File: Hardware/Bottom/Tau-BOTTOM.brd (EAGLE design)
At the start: 33 x 33 mm, 31 parts, among them U1 AD5242-SO16

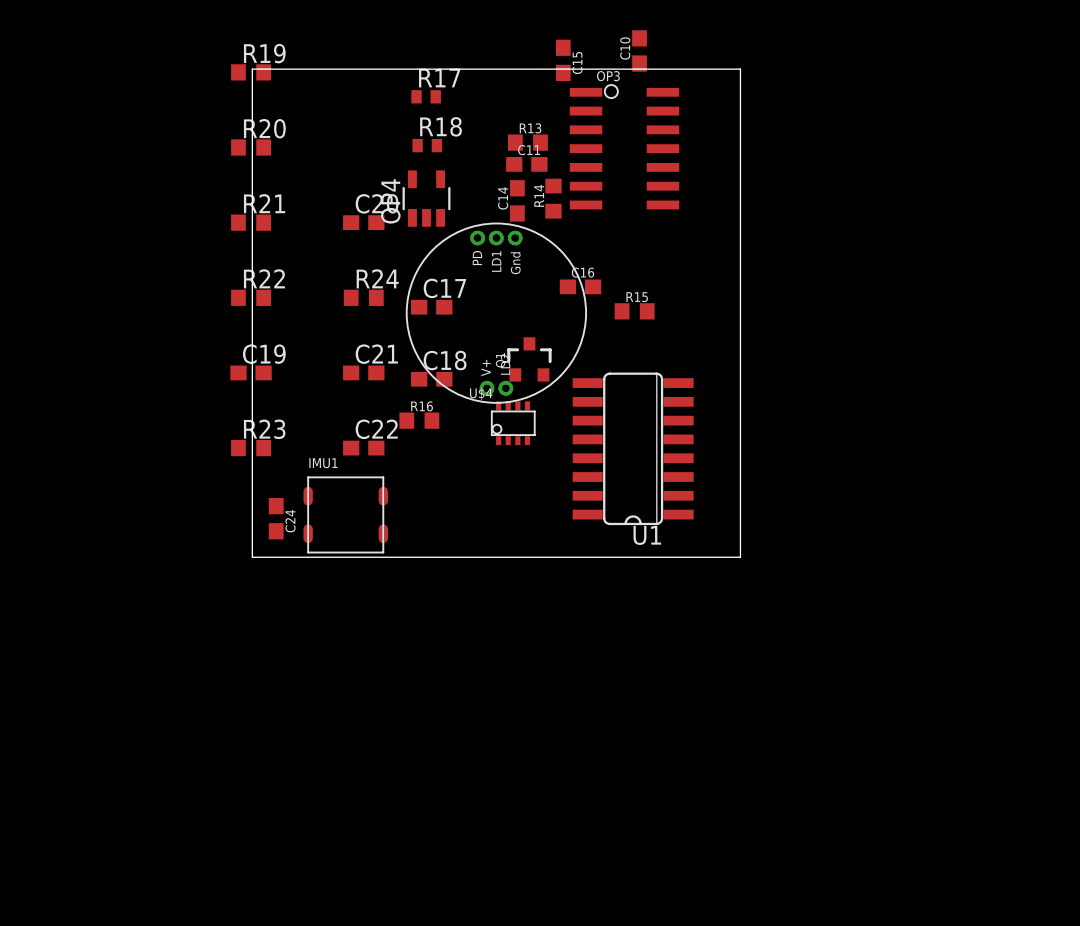
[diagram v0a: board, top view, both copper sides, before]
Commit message: Changes committed to top and bottom board
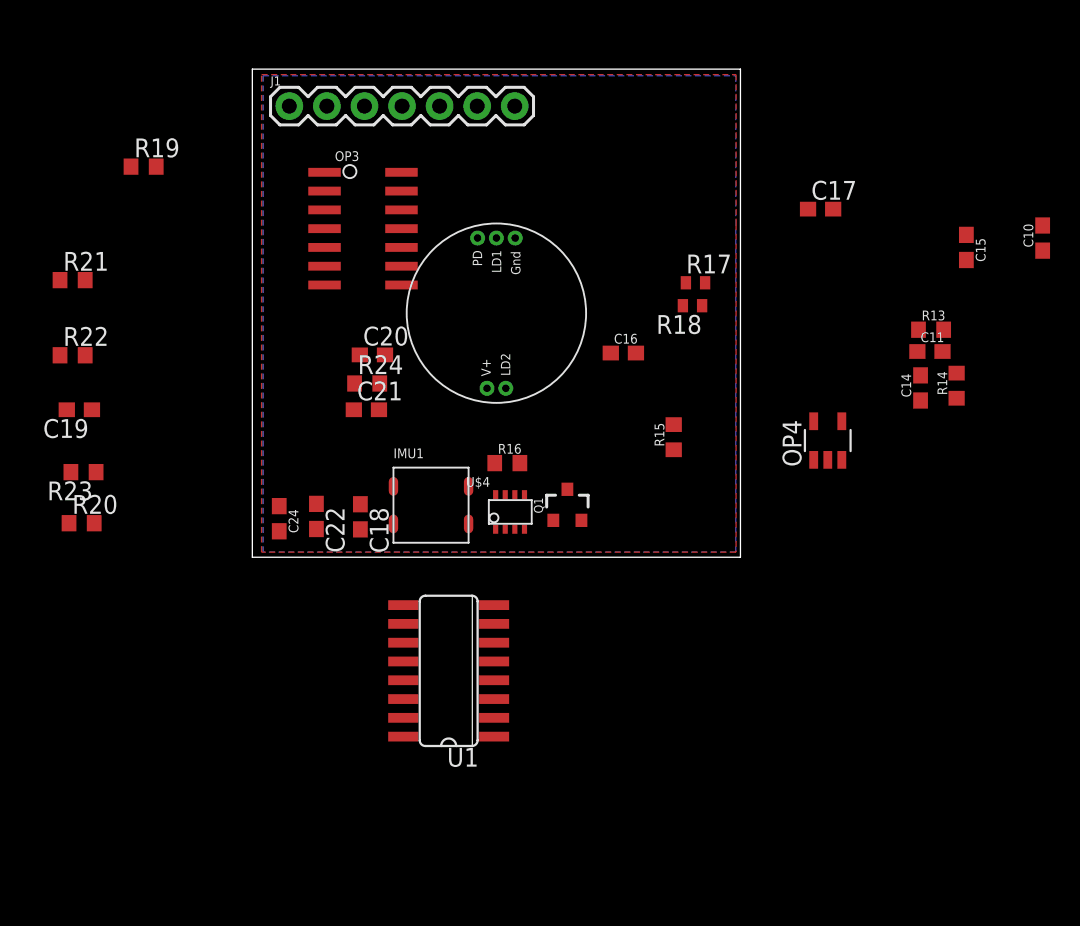
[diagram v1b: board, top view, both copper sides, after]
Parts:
- added J1: (no value), LinnesLab-Connectors:1X07
- moved OP4 31.7 mm to (41.4, 10.4)
- moved C11 30.0 mm to (48.3, 16.4)
- moved C14 30.0 mm to (47.7, 13.9)
- moved C15 30.0 mm to (50.8, 23.4)
- moved R13 30.0 mm to (48.4, 17.9)
- moved C10 30.0 mm to (55.9, 24.1)
- moved R14 30.0 mm to (50.1, 14.1)
- moved R20 27.9 mm to (-9.04, 4.80)
- moved C17 27.1 mm to (40.9, 26.0)
- moved R17 22.1 mm to (32.5, 21.1)
- moved R18 20.9 mm to (32.3, 19.5), turned to 180 degrees
- moved U1 19.5 mm to (15.8, -5.18)
- moved OP3 18.5 mm to (9.98, 24.7)
- moved R21 12.7 mm to (-9.65, 21.2)
- moved R22 12.7 mm to (-9.65, 16.2)
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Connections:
- removed net LED.CTRL: U$4.8
- removed net TIA: C10.2, C15.1, OP4.1, U1.3
- new net A6/TIA: C10.2, C15.1, J1.5, OP4.1, U1.3
- new net A7/PPG: C21.2, J1.7, OP3.1
- new net D29/LED.CTRL: J1.6, U$4.8
- net PPG: no longer C21.2, OP3.1
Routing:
- added copper zone on layer 1, net 3.3V
- added copper zone on layer 16, net GND

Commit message: Bottom board nearly routed
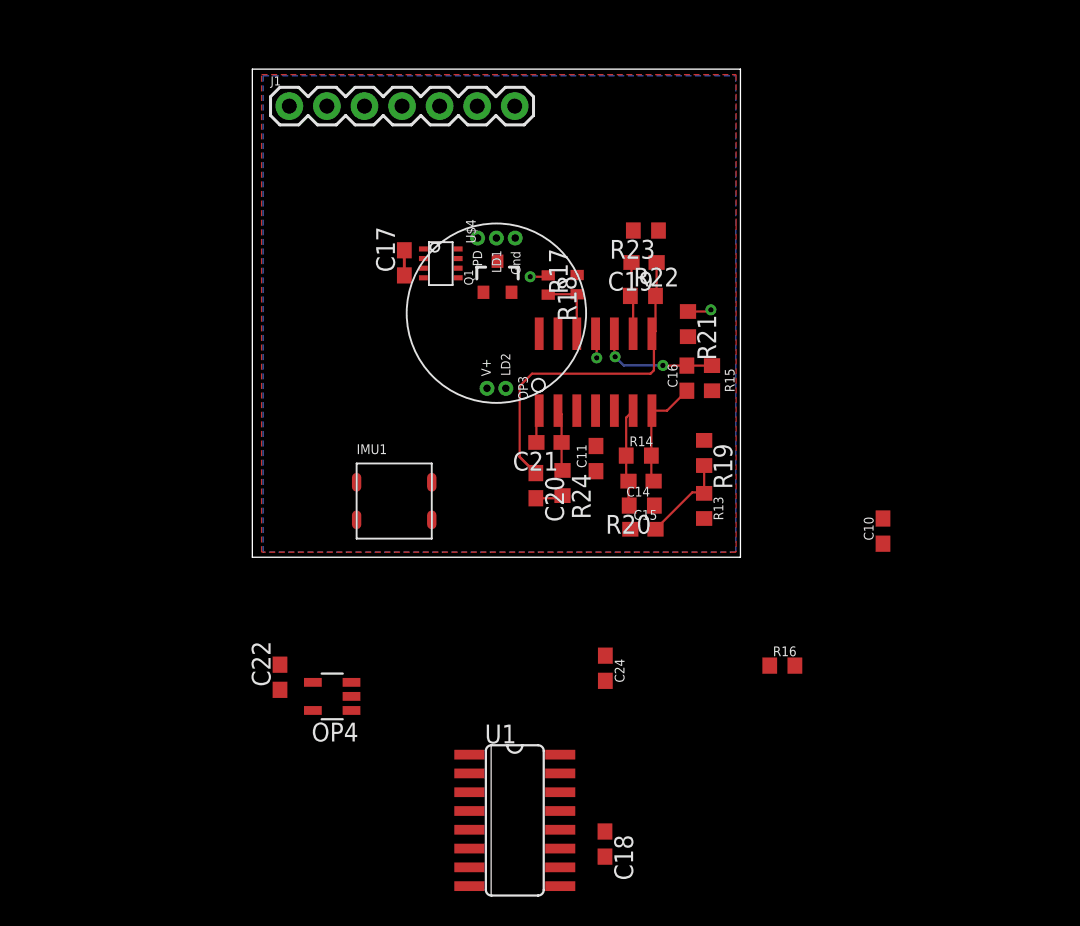
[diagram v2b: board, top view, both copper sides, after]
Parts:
- moved R19 42.6 mm to (33.0, 9.55), turned to 270 degrees
- moved R21 41.7 mm to (32.0, 18.3), turned to 270 degrees
- moved R23 41.4 mm to (29.1, 24.6)
- moved C19 39.5 mm to (29.0, 22.4)
- moved R22 38.8 mm to (28.9, 20.2)
- moved R20 37.9 mm to (28.8, 5.99), turned to 180 degrees
- moved OP4 37.7 mm to (7.90, -6.91), turned to 90 degrees
- moved C15 29.0 mm to (28.9, 4.39), turned to 0 degrees
- moved C17 28.4 mm to (12.8, 22.4), turned to 90 degrees
- moved C18 27.6 mm to (26.3, -16.9)
- moved C24 24.3 mm to (26.4, -5.00)
- moved C11 23.7 mm to (25.7, 9.17), turned to 90 degrees
- moved R16 23.1 mm to (38.3, -4.83)
- moved C10 22.6 mm to (45.1, 4.27)
- moved R14 22.0 mm to (28.6, 9.37), turned to 0 degrees
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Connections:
- removed net LED: Q1.3
- net LED.C: now also Q1.3
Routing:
- net N$19: track 0.00 -> 24.9 mm
- net N$17: track 0.00 -> 8.38 mm, vias 0 -> 2
- net N$16: track 0.00 -> 7.80 mm
- net N$15: track 0.00 -> 6.70 mm
- net GND: track 0.00 -> 6.21 mm, vias 0 -> 3
- net N$13: track 0.00 -> 6.20 mm
- net N$18: track 0.00 -> 4.93 mm
- net N$10: track 0.00 -> 4.65 mm
- net G.W2: track 0.00 -> 4.17 mm
- net A7/PPG: track 0.00 -> 2.23 mm
- net N$20: track 0.00 -> 1.88 mm

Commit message: More routing changes to bottom board
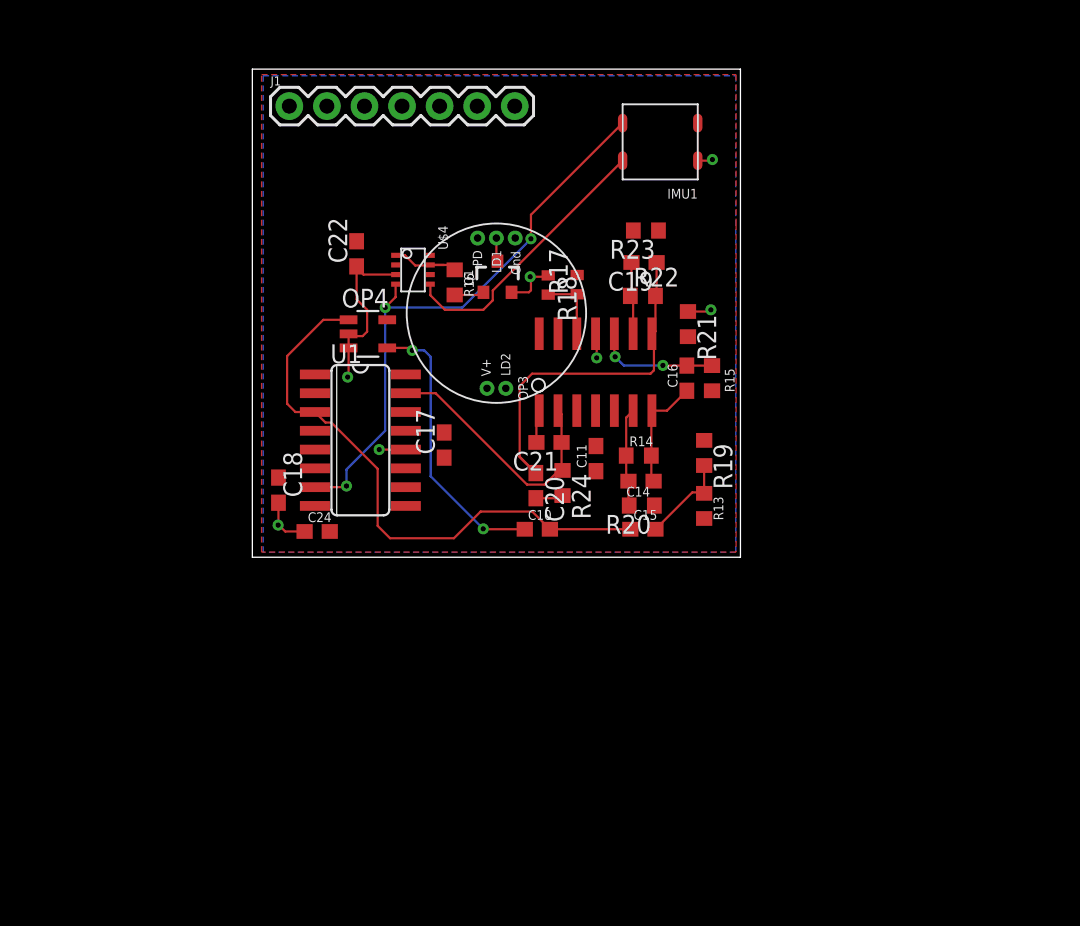
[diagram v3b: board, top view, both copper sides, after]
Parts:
- moved R16 34.1 mm to (16.2, 21.1), turned to 270 degrees
- moved C18 32.6 mm to (4.27, 7.04), turned to 90 degrees
- moved IMU1 30.2 mm to (30.1, 30.6), turned to 180 degrees
- moved C22 29.1 mm to (9.55, 23.0)
- moved U1 27.7 mm to (9.80, 10.4)
- moved OP4 24.6 mm to (10.3, 17.6), turned to 270 degrees
- moved C10 23.4 mm to (21.8, 4.39), turned to 0 degrees
- moved C24 21.6 mm to (6.88, 4.24), turned to 0 degrees
- moved C17 12.6 mm to (15.5, 10.1)
- moved U$4 1.93 mm to (13.4, 21.9)
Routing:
- net SCL: track 0.00 -> 39.4 mm, vias 0 -> 3
- net A6/TIA: track 0.00 -> 38.9 mm
- net PD.C: track 0.00 -> 19.1 mm, vias 0 -> 2
- net GND: track 6.21 -> 25.0 mm, vias 3 -> 7
- net SDA: track 0.00 -> 18.7 mm
- net G.W2: track 4.17 -> 17.7 mm
- net N$9: track 0.00 -> 5.35 mm
- net N$8: track 0.00 -> 2.02 mm
- net LED.C: track 0.00 -> 1.60 mm

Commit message: Changes made to top and bottom board
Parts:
- removed J1: (no value), LinnesLab-Connectors:1X07
- added C1: 100n, LinnesLab-Passives:C0603
- added J2: (no value), LinnesLab-Connectors:1X07_1.27MM
- moved IMU1 23.9 mm to (6.27, 28.6), turned to 90 degrees
- moved C17 17.0 mm to (6.30, 24.4), turned to 0 degrees
- moved C24 16.3 mm to (6.22, 20.5), turned to 180 degrees
- moved C10 14.6 mm to (16.6, 18.0), turned to 180 degrees
- moved R16 8.92 mm to (19.0, 29.5), turned to 0 degrees
- moved OP4 7.27 mm to (16.6, 21.2), turned to 0 degrees
- moved U$4 7.01 mm to (7.72, 17.8), turned to 180 degrees
- moved Q1 5.51 mm to (19.0, 26.9), turned to 180 degrees
- moved C22 5.39 mm to (14.1, 20.2), turned to 270 degrees
- moved C18 3.96 mm to (7.37, 4.57), turned to 0 degrees
- moved C15 3.51 mm to (25.4, 4.65)
- moved R23 2.06 mm to (27.1, 24.1), turned to 0 degrees
- moved U1 0.69 mm to (10.5, 10.5)
- moved C16 0.23 mm to (31.6, 14.6)
- moved R15 0.23 mm to (33.4, 14.6)
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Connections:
- removed net PPG: U1.14
- net 3.3V: now also J2.4
- net A6/TIA: now also J2.6; no longer J1.5
- net A7/PPG: now also J2.7, U1.14; no longer J1.7
- net D29/LED.CTRL: now also J2.5; no longer J1.6
- net GND: now also C1.1, J2.3
- net SCL: now also J2.2
- net SDA: now also J2.1
- net VREF: now also C1.2
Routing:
- net A7/PPG: track 2.23 -> 52.5 mm, vias 0 -> 2
- net VREF: track 0.00 -> 32.2 mm, vias 0 -> 5
- net D29/LED.CTRL: track 0.00 -> 17.4 mm, vias 0 -> 2
- net N$13: track 6.20 -> 21.1 mm, vias 0 -> 2
- net N$9: track 5.35 -> 18.3 mm
- net SDA: track 18.7 -> 31.4 mm, vias 0 -> 2
- net GND: track 25.0 -> 37.6 mm, vias 7 -> 12
- net A6/TIA: track 38.9 -> 50.0 mm, vias 0 -> 4
- net SCL: track 39.4 -> 28.9 mm, vias 3 -> 2
- net PD.C: track 19.1 -> 22.8 mm
- net N$19: track 24.9 -> 23.0 mm
- net N$17: track 8.38 -> 10.2 mm
- net N$18: track 4.93 -> 6.68 mm
- net G.W2: track 17.7 -> 16.8 mm, vias 0 -> 2

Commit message: Changes made to top and bottom board
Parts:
- added C2: 1u, LinnesLab-Passives:C0603
- added U3: PCF8523, LinnesLab-Clocks:SO8
- added XTAL2: 32.7680kHz, LinnesLab-Clocks:2-SMD.NOLEAD.2.0MMTO1.2MM
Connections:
- new net N$12: U3.2, XTAL2.P$1
- new net N$4: U3.1, XTAL2.P$2
- new net VBAT: U3.3
- net 3.3V: now also C2.1, U3.8
- net GND: now also C2.2, U3.4
- net SCL: now also U3.6
- net SDA: now also U3.5

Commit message: Finished Bottom and Top boards' first version
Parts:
- moved XTAL2 50.1 mm to (32.5, 29.2), turned to 270 degrees
- moved C2 46.2 mm to (32.4, 32.0), turned to 90 degrees
- moved U3 45.7 mm to (28.0, 30.9), turned to 180 degrees
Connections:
- net A6/TIA renamed A5/TIA
- net A7/PPG renamed A4/PPG
- net D29/LED.CTRL renamed D30/LED.CTRL
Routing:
- net SDA: track 31.4 -> 54.0 mm, vias 2 -> 3
- net SCL: track 28.9 -> 50.8 mm, vias 2 -> 3
- net GND: track 37.6 -> 40.7 mm, vias 12 -> 14
- net N$4: track 0.00 -> 2.10 mm
- net N$12: track 0.00 -> 1.96 mm
- net VREF: track 32.2 -> 33.4 mm
